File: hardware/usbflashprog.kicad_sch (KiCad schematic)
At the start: 13 parts, among them J1 12-18V, J2 Parallel Adapter, J3 Serial Adapter, U1 7809

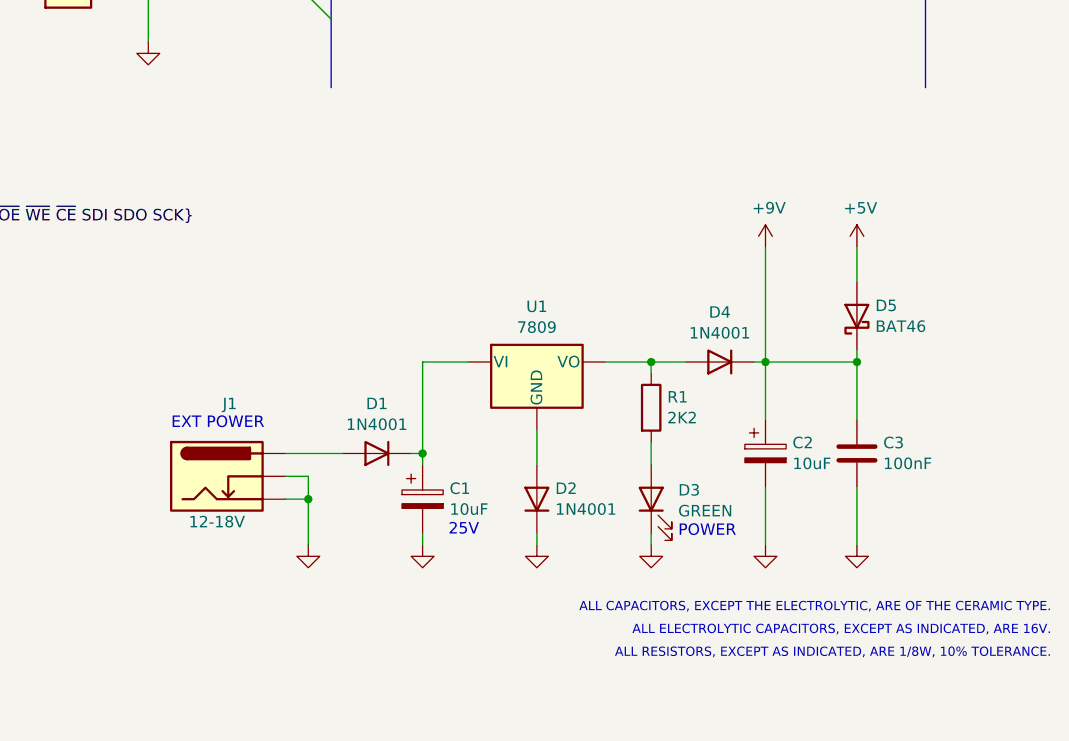
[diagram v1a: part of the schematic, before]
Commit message: Rev.G. Change external power supply to a MT3606 DC-DC Module
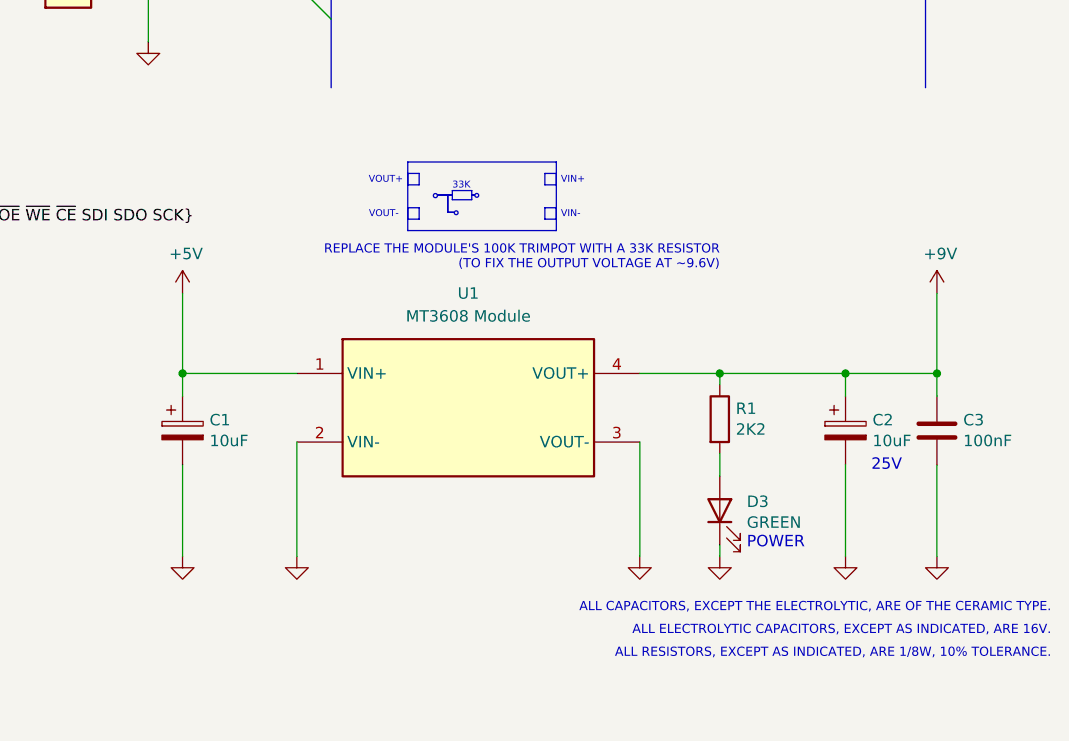
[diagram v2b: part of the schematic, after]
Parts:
- removed D1, D2, D4: 1N4001, Diode_THT:D_DO-41_SOD81_P10.16mm_Horizontal, symbol Diode:1N4001
- removed D5: BAT46, Diode_THT:D_DO-35_SOD27_P7.62mm_Horizontal, symbol Diode:BAT46
- removed J1: 12-18V, Connector_BarrelJack:BarrelJack_Horizontal, symbol Connector:Barrel_Jack_Switch
- removed U1: 7809, Package_TO_SOT_THT:TO-220-3_Vertical, symbol Regulator_Linear:LM7809_TO220
- added U1: MT3608 Module, DC2DC_Modules:MT3608_module, symbol DC2DC_Modules:MT3608_Module
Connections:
- net +5V: now also C1.1, U1.1 (VIN+)
- net +9V: now also R1.1, U1.4 (VOUT+)
- net GND: now also U1.2 (VIN-), U1.3 (VOUT-)
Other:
- note added: "33K"
- note added: "REPLACE THE MODULE'S 100K TRIMPOT WITH A 33K RESISTOR (TO FIX THE OUTPUT VOLTAGE AT ~9.6V)"
- note added: "VIN+"
- note added: "VIN-"
- note added: "VOUT+"
- note added: "VOUT-"
- note removed: "EXT POWER"
